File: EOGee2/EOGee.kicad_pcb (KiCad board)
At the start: 2 copper layers, 79 x 60.7 mm, 78 parts, among them J101 USB_B_Micro, J102 AudioJack3, J103 AudioJack2, J104 AudioJack2, J105 AudioJack2, J106 Conn_01x02, SW101 SW_Push_45deg, SW102 SW_Push_45deg, U101 LMV358, U102 AD8226ARMZ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

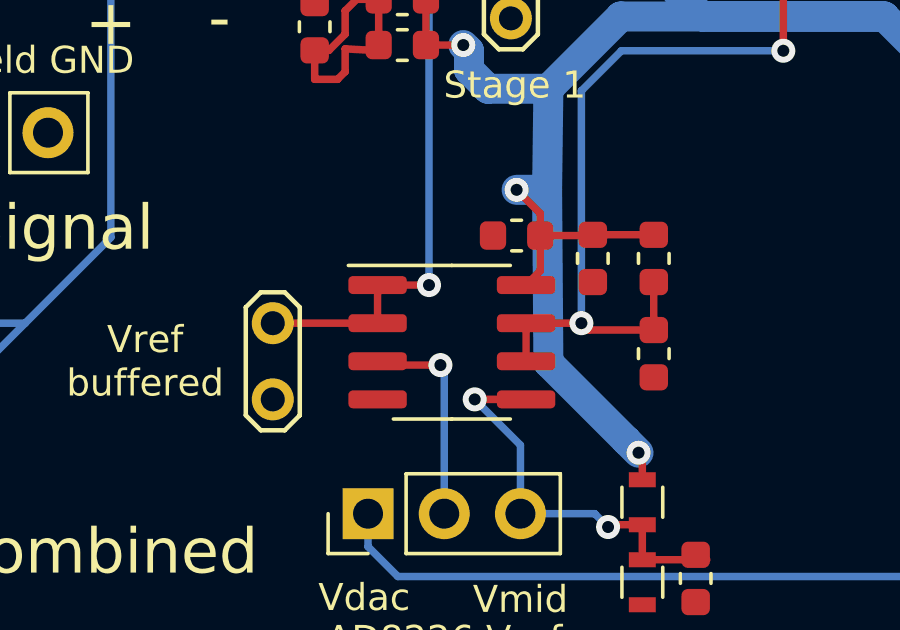
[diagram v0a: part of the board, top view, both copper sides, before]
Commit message: replace OP2177 with LMV358 because does not support 3.3V rail
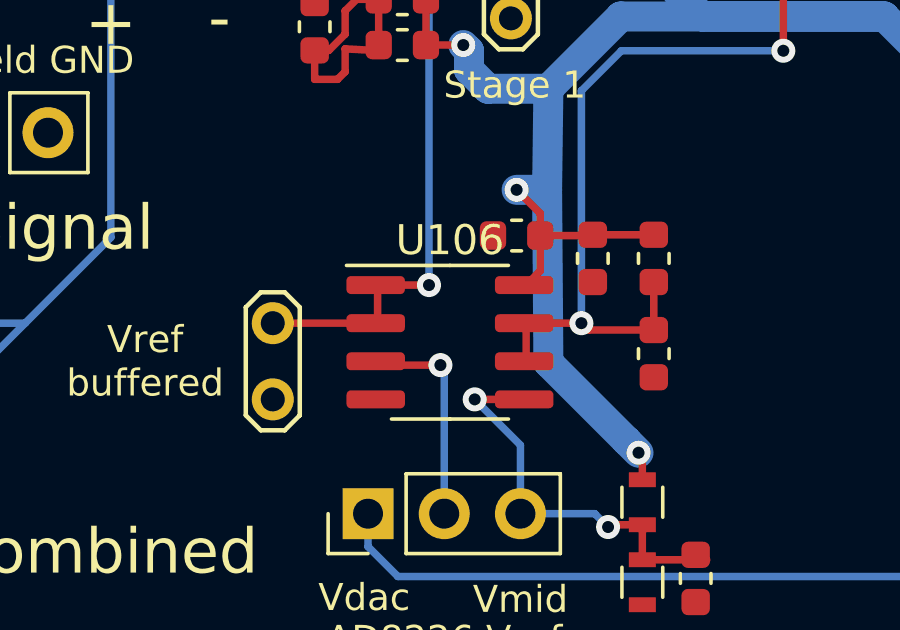
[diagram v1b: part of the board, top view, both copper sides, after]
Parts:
- U106: value OP2177ARZ-REEL -> LMV358
- moved U106 0.06 mm to (104.6, 61.6)
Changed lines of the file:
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@@
   )
   (module Package_SO:SOIC-8_3.9x4.9mm_P1.27mm (layer F.Cu)
-    (at 104.648 61.595)
-    (descr "SOIC, 8 Pin (JEDEC MS-012AA, https://www.analog.com/media/en/package-pcb-resources/package/pkg_pdf/soic_narrow-r/r_8.pdf), generated with kicad-footprint-generator ipc_gullwing_generator.py")
-    (tags "SOIC SO")
-    (attr smd)
-    (fp_text reference U106 (at 0 -3.4) (layer F.SilkS) hide
-      (effects (font (size 1 1) (thickness 0.15)))
-    )
-    (fp_text value OP2177ARZ-REEL (at 0 3.4) (layer F.Fab)
-      (effects (font (size 1 1) (thickness 0.15)))
-    )
-    (fp_text user %R (at 0 0) (layer F.Fab)
-      (effects (font (size 0.98 0.98) (thickness 0.15)))
-    )
-    (fp_line (start 3.7 -2.7) (end -3.7 -2.7) (layer F.CrtYd) (width 0.05))
-    (fp_line (start 3.7 2.7) (end 3.7 -2.7) (layer F.CrtYd) (width 0.05))
-    (fp_line (start -3.7 2.7) (end 3.7 2.7) (layer F.CrtYd) (width 0.05))
-    (fp_line (start -3.7 -2.7) (end -3.7 2.7) (layer F.CrtYd) (width 0.05))
-    (fp_line (start -1.95 -1.475) (end -0.975 -2.45) (layer F.Fab) (width 0.1))
-    (fp_line (start -1.95 2.45) (end -1.95 -1.475) (layer F.Fab) (width 0.1))
-    (fp_line (start 1.95 2.45) (end -1.95 2.45) (layer F.Fab) (width 0.1))
-    (fp_line (start 1.95 -2.45) (end 1.95 2.45) (layer F.Fab) (width 0.1))
-    (fp_line (start -0.975 -2.45) (end 1.95 -2.45) (layer F.Fab) (width 0.1))
-    (fp_line (start 0 -2.56) (end -3.45 -2.56) (layer F.SilkS) (width 0.12))
-    (fp_line (start 0 -2.56) (end 1.95 -2.56) (layer F.SilkS) (width 0.12))
-    (fp_line (start 0 2.56) (end -1.95 2.56) (layer F.SilkS) (width 0.12))
-    (fp_line (start 0 2.56) (end 1.95 2.56) (layer F.SilkS) (width 0.12))
-    (pad 8 smd roundrect (at 2.475 -1.905) (size 1.95 0.6) (layers F.Cu F.Paste F.Mask) (roundrect_rratio 0.25)
-      (net 2 +3.3VA))
-    (pad 7 smd roundrect (at 2.475 -0.635) (size 1.95 0.6) (layers F.Cu F.Paste F.Mask) (roundrect_rratio 0.25)
-      (net 11 "Net-(C105-Pad2)"))
-    (pad 6 smd roundrect (at 2.475 0.635) (size 1.95 0.6) (layers F.Cu F.Paste F.Mask) (roundrect_rratio 0.25)
-      (net 11 "Net-(C105-Pad2)"))
-    (pad 5 smd roundrect (at 2.475 1.905) (size 1.95 0.6) (layers F.Cu F.Paste F.Mask) (roundrect_rratio 0.25)
-      (net 69 "Net-(C122-Pad1)"))
-    (pad 4 smd roundrect (at -2.475 1.905) (size 1.95 0.6) (layers F.Cu F.Paste F.Mask) (roundrect_rratio 0.25)
-      (net 1 GND))
-    (pad 3 smd roundrect (at -2.475 0.635) (size 1.95 0.6) (layers F.Cu F.Paste F.Mask) (roundrect_rratio 0.25)
-      (net 31 "Net-(JP105-Pad2)"))
-    (pad 2 smd roundrect (at -2.475 -0.635) (size 1.95 0.6) (layers F.Cu F.Paste F.Mask) (roundrect_rratio 0.25)
-      (net 36 "Net-(TP104-Pad1)"))
-    (pad 1 smd roundrect (at -2.475 -1.905) (size 1.95 0.6) (layers F.Cu F.Paste F.Mask) (roundrect_rratio 0.25)
-      (net 36 "Net-(TP104-Pad1)"))
-    (model ${KISYS3DMOD}/Package_SO.3dshapes/SOIC-8_3.9x4.9mm_P1.27mm.wrl
-      (at (xyz 0 0 0))
-      (scale (xyz 1 1 1))
-      (rotate (xyz 0 0 0))
-    )
-  )
-  (module Package_SO:SOIC-8_3.9x4.9mm_P1.27mm (layer F.Cu)
     (at 115.062 45.212 90)
     (descr "SOIC, 8 Pin (JEDEC MS-012AA, https://www.analog.com/media/en/package-pcb-resources/package/pkg_pdf/soic_narrow-r/r_8.pdf), generated with kicad-footprint-generator ipc_gullwing_generator.py")
@@
     )
   )
+  (module Package_SO:SOIC-8_3.9x4.9mm_P1.27mm (layer F.Cu)
+    (at 104.5845 61.595)
+    (descr "SOIC, 8 Pin (JEDEC MS-012AA, https://www.analog.com/media/en/package-pcb-resources/package/pkg_pdf/soic_narrow-r/r_8.pdf), generated with kicad-footprint-generator ipc_gullwing_generator.py")
+    (tags "SOIC SO")
+    (attr smd)
+    (fp_text reference U106 (at 0 -3.4) (layer F.SilkS)
+      (effects (font (size 1 1) (thickness 0.15)))
+    )
+    (fp_text value LMV358 (at 0 3.4) (layer F.Fab)
+      (effects (font (size 1 1) (thickness 0.15)))
+    )
+    (fp_line (start 0 2.56) (end 1.95 2.56) (layer F.SilkS) (width 0.12))
+    (fp_line (start 0 2.56) (end -1.95 2.56) (layer F.SilkS) (width 0.12))
+    (fp_line (start 0 -2.56) (end 1.95 -2.56) (layer F.SilkS) (width 0.12))
+    (fp_line (start 0 -2.56) (end -3.45 -2.56) (layer F.SilkS) (width 0.12))
+    (fp_line (start -0.975 -2.45) (end 1.95 -2.45) (layer F.Fab) (width 0.1))
+    (fp_line (start 1.95 -2.45) (end 1.95 2.45) (layer F.Fab) (width 0.1))
+    (fp_line (start 1.95 2.45) (end -1.95 2.45) (layer F.Fab) (width 0.1))
+    (fp_line (start -1.95 2.45) (end -1.95 -1.475) (layer F.Fab) (width 0.1))
+    (fp_line (start -1.95 -1.475) (end -0.975 -2.45) (layer F.Fab) (width 0.1))
+    (fp_line (start -3.7 -2.7) (end -3.7 2.7) (layer F.CrtYd) (width 0.05))
+    (fp_line (start -3.7 2.7) (end 3.7 2.7) (layer F.CrtYd) (width 0.05))
+    (fp_line (start 3.7 2.7) (end 3.7 -2.7) (layer F.CrtYd) (width 0.05))
+    (fp_line (start 3.7 -2.7) (end -3.7 -2.7) (layer F.CrtYd) (width 0.05))
+    (fp_text user %R (at 0 0) (layer F.Fab)
+      (effects (font (size 0.98 0.98) (thickness 0.15)))
+    )
+    (pad 1 smd roundrect (at -2.475 -1.905) (size 1.95 0.6) (layers F.Cu F.Paste F.Mask) (roundrect_rratio 0.25)
+      (net 36 "Net-(TP104-Pad1)"))
+    (pad 2 smd roundrect (at -2.475 -0.635) (size 1.95 0.6) (layers F.Cu F.Paste F.Mask) (roundrect_rratio 0.25)
+      (net 36 "Net-(TP104-Pad1)"))
+    (pad 3 smd roundrect (at -2.475 0.635) (size 1.95 0.6) (layers F.Cu F.Paste F.Mask) (roundrect_rratio 0.25)
+      (net 31 "Net-(JP105-Pad2)"))
+    (pad 4 smd roundrect (at -2.475 1.905) (size 1.95 0.6) (layers F.Cu F.Paste F.Mask) (roundrect_rratio 0.25)
+      (net 1 GND))
+    (pad 5 smd roundrect (at 2.475 1.905) (size 1.95 0.6) (layers F.Cu F.Paste F.Mask) (roundrect_rratio 0.25)
+      (net 69 "Net-(C122-Pad1)"))
+    (pad 6 smd roundrect (at 2.475 0.635) (size 1.95 0.6) (layers F.Cu F.Paste F.Mask) (roundrect_rratio 0.25)
+      (net 11 "Net-(C105-Pad2)"))
+    (pad 7 smd roundrect (at 2.475 -0.635) (size 1.95 0.6) (layers F.Cu F.Paste F.Mask) (roundrect_rratio 0.25)
+      (net 11 "Net-(C105-Pad2)"))
+    (pad 8 smd roundrect (at 2.475 -1.905) (size 1.95 0.6) (layers F.Cu F.Paste F.Mask) (roundrect_rratio 0.25)
+      (net 2 +3.3VA))
+    (model ${KISYS3DMOD}/Package_SO.3dshapes/SOIC-8_3.9x4.9mm_P1.27mm.wrl
+      (at (xyz 0 0 0))
+      (scale (xyz 1 1 1))
+      (rotate (xyz 0 0 0))
+    )
+  )
   (gr_text Reset (at 137.16 24.892) (layer F.SilkS)
     (effects (font (size 0.75 0.75) (thickness 0.125)))
@@
     (connect_pads (clearance 0.1524))
     (min_thickness 0.1524)
-    (fill (arc_segments 32) (thermal_gap 0.25) (thermal_bridge_width 0.25))
+    (fill yes (arc_segments 32) (thermal_gap 0.25) (thermal_bridge_width 0.25))
     (polygon
       (pts
@@
     (connect_pads (clearance 0.2))
     (min_thickness 0.254)
-    (fill (arc_segments 32) (thermal_gap 0.508) (thermal_bridge_width 0.508))
+    (fill yes (arc_segments 32) (thermal_gap 0.508) (thermal_bridge_width 0.508))
     (polygon
       (pts
